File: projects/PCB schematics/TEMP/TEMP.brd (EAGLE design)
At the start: 0 parts

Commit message: POWER - Initial drafts.
Adding in initial place holders for DCDC, 5V, and 12V. Completed most of TEMP.
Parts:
- added IC1, IC10, IC2, IC3, IC4, IC5, IC6, IC7, IC8, IC9: 4051D, 40xx:SO16
- added J1, J2: SAMTEC-TFM-120-02-X-D-LCJ, SAMTEC-TFM-120-02-X-D-LC:SAMTEC-TFM-120-02-X-D-LC
- added R1, R2, R3, R4: (no value), rcl:R0805
- added X2: 5566-4, con-molex:5566-4
- added X3: 5566-2, con-molex:5566-2
- added X4: 5566-10, con-molex:5566-10
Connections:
- new net CS_A: IC1.11, IC10.11, IC2.11, IC3.11, IC4.11, IC5.11, IC6.11, IC7.11, IC8.11, IC9.11, R2.2, X2.1
- new net CS_B: IC1.10, IC10.10, IC2.10, IC3.10, IC4.10, IC5.10, IC6.10, IC7.10, IC8.10, IC9.10, R3.2, X2.2
- new net CS_C: IC1.9, IC10.9, IC2.9, IC3.9, IC4.9, IC5.9, IC6.9, IC7.9, IC8.9, IC9.9, R4.2, X2.3
- new net GND: IC1.8, IC10.8, IC2.8, IC3.8, IC4.8, IC5.8, IC6.8, IC7.8, IC8.8, IC9.8, R1.1, R2.1, R3.1, R4.1, X3.2
- new net INH: IC1.6, IC10.6, IC2.6, IC3.6, IC4.6, IC5.6, IC6.6, IC7.6, IC8.6, IC9.6, R1.2
- new net TEMP1: IC1.13, J1.1
- new net TEMP10: IC2.14, J1.10
- new net TEMP11: IC2.15, J1.11
- new net TEMP12: IC2.12, J1.12
- new net TEMP13: IC2.1, J1.13
- new net TEMP14: IC2.5, J1.14
- new net TEMP15: IC2.2, J1.15
- new net TEMP16: IC2.4, J1.16
- new net TEMP17: IC3.13, J1.17
- new net TEMP18: IC3.14, J1.18
- new net TEMP19: IC3.15, J1.19
- new net TEMP2: IC1.14, J1.2
- new net TEMP20: IC3.12, J1.20
- new net TEMP21: IC3.1, J1.21
- new net TEMP22: IC3.5, J1.22
- new net TEMP23: IC3.2, J1.23
- new net TEMP24: IC3.4, J1.24
- new net TEMP25: IC5.13, J1.25
- new net TEMP26: IC5.14, J1.26
- new net TEMP27: IC5.15, J1.27
- new net TEMP28: IC5.12, J1.28
- new net TEMP29: IC5.1, J1.29
- new net TEMP3: IC1.15, J1.3
- new net TEMP30: IC5.5, J1.30
- new net TEMP31: IC5.2, J1.31
- new net TEMP32: IC5.4, J1.32
- new net TEMP33: IC6.13, J1.33
- new net TEMP34: IC6.14, J1.34
- new net TEMP35: IC6.15, J1.35
- new net TEMP36: IC6.12, J1.36
- new net TEMP37: IC6.1, J1.37
- new net TEMP38: IC6.5, J1.38
- new net TEMP39: IC6.2, J1.39
- new net TEMP4: IC1.12, J1.4
- new net TEMP40: IC6.4, J1.40
- new net TEMP41: IC7.13, J2.1
- new net TEMP42: IC7.14, J2.2
- new net TEMP43: IC7.15, J2.3
- new net TEMP44: IC7.12, J2.4
- new net TEMP45: IC7.1, J2.5
- new net TEMP46: IC7.5, J2.6
- new net TEMP47: IC7.2, J2.7
- new net TEMP48: IC7.4, J2.8
- new net TEMP49: IC4.13, J2.9
- new net TEMP5: IC1.1, J1.5
- new net TEMP50: IC4.14, J2.10
- new net TEMP51: IC4.15, J2.11
- new net TEMP52: IC4.12, J2.12
- new net TEMP53: IC4.1, J2.13
- new net TEMP54: IC4.5, J2.14
- new net TEMP55: IC4.2, J2.15
- new net TEMP56: IC4.4, J2.16
- new net TEMP57: IC9.13, J2.17
- new net TEMP58: IC9.14, J2.18
- new net TEMP59: IC9.15, J2.19
- new net TEMP6: IC1.5, J1.6
- new net TEMP60: IC9.12, J2.20
- new net TEMP61: IC9.1, J2.21
- new net TEMP62: IC9.5, J2.22
- new net TEMP63: IC9.2, J2.23
- new net TEMP64: IC9.4, J2.24
- new net TEMP65: IC8.13, J2.25
- new net TEMP66: IC8.14, J2.26
- new net TEMP67: IC8.15, J2.27
- new net TEMP68: IC8.12, J2.28
- new net TEMP69: IC8.1, J2.29
- new net TEMP7: IC1.2, J1.7
- new net TEMP70: IC8.5, J2.30
- new net TEMP71: IC8.2, J2.31
- new net TEMP72: IC8.4, J2.32
- new net TEMP73: IC10.13, J2.33
- new net TEMP74: IC10.14, J2.34
- new net TEMP75: IC10.15, J2.35
- new net TEMP76: IC10.12, J2.36
- new net TEMP77: IC10.1, J2.37
- new net TEMP78: IC10.5, J2.38
- new net TEMP79: IC10.2, J2.39
- new net TEMP8: IC1.4, J1.8
- new net TEMP80: IC10.4, J2.40
- new net TEMP9: IC2.13, J1.9
- new net TEMP_OUT1: IC1.3, X4.1
- new net TEMP_OUT10: IC10.3, X4.10
- new net TEMP_OUT2: IC2.3, X4.2
- new net TEMP_OUT3: IC3.3, X4.3
- new net TEMP_OUT4: IC5.3, X4.4
- new net TEMP_OUT5: IC6.3, X4.5
- new net TEMP_OUT6: IC7.3, X4.6
- new net TEMP_OUT7: IC4.3, X4.7
- new net TEMP_OUT8: IC9.3, X4.8
- new net TEMP_OUT9: IC8.3, X4.9
- new net VCC: IC1.16, IC10.16, IC2.16, IC3.16, IC4.16, IC5.16, IC6.16, IC7.16, IC8.16, IC9.16, X3.1
- new net VEE: IC1.7, IC10.7, IC2.7, IC3.7, IC4.7, IC5.7, IC6.7, IC7.7, IC8.7, IC9.7
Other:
- board outline added: 78.7 x 64.8 mm

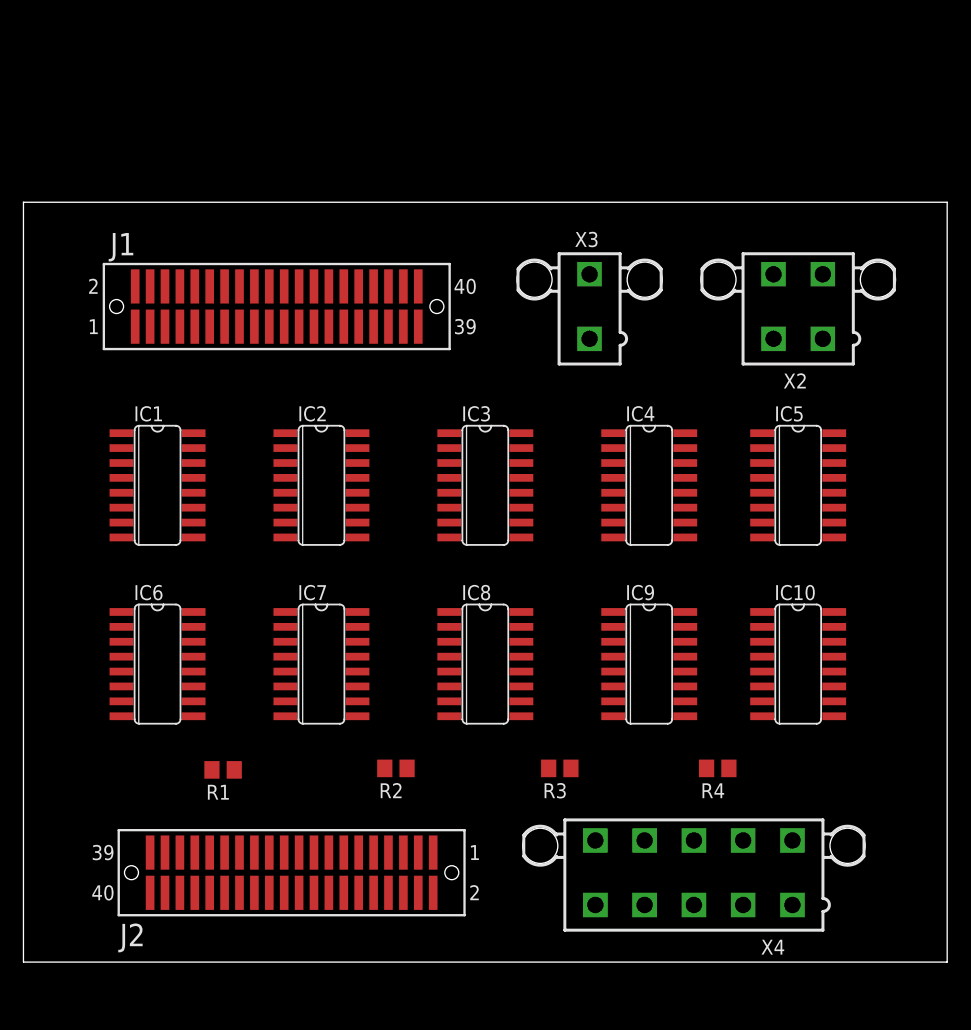
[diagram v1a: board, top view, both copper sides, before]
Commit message: PROJ - Added IMD, OUTPUT.
Additional changes made to INPUT.
OUTPUT board added for ECU/motor controller signal processing.
IMD added for IMD fuse board. Rules may require fusing IMD. Might as well.
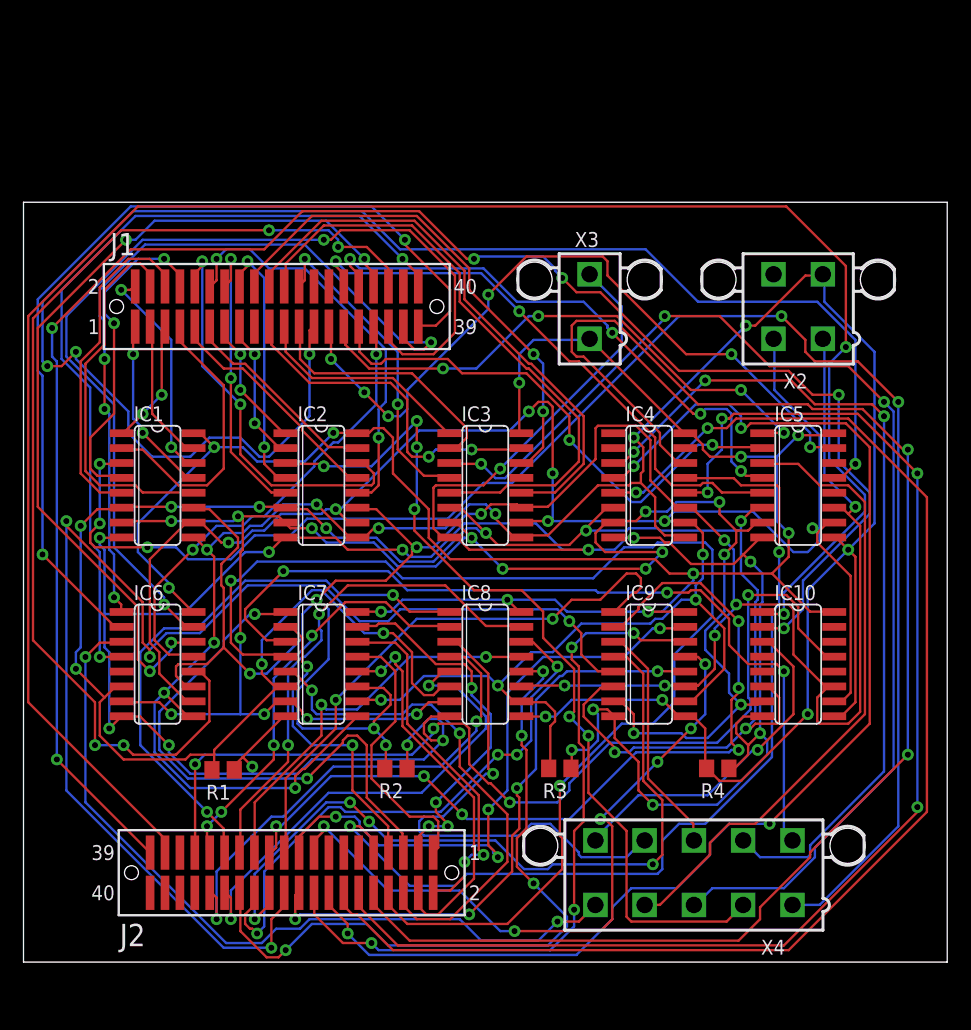
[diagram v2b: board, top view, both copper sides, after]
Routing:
- net GND: track 0.00 -> 240.1 mm, vias 0 -> 16
- net CS_C: track 0.00 -> 215.0 mm, vias 0 -> 13
- net CS_A: track 0.00 -> 205.5 mm, vias 0 -> 12
- net CS_B: track 0.00 -> 199.0 mm, vias 0 -> 11
- net INH: track 0.00 -> 187.8 mm, vias 0 -> 12
- net VCC: track 0.00 -> 171.8 mm, vias 0 -> 11
- net TEMP77: track 0.00 -> 162.7 mm, vias 0 -> 2
- net VEE: track 0.00 -> 158.2 mm, vias 0 -> 17
- net TEMP79: track 0.00 -> 152.1 mm, vias 0 -> 6
- net TEMP_OUT1: track 0.00 -> 138.6 mm, vias 0 -> 5
- net TEMP25: track 0.00 -> 134.1 mm, vias 0 -> 4
- net TEMP50: track 0.00 -> 131.0 mm, vias 0 -> 2
- net TEMP54: track 0.00 -> 116.3 mm, vias 0 -> 2
- net TEMP62: track 0.00 -> 113.0 mm, vias 0 -> 4
- net TEMP52: track 0.00 -> 111.4 mm, vias 0 -> 4
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
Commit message: TEMP - Initial board placement.
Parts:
- removed IC1, IC10, IC2, IC3, IC4, IC5, IC6, IC7, IC8, IC9: 4051D, 40xx:SO16
- removed J2: SAMTEC-TFM-120-02-X-D-LCJ, SAMTEC-TFM-120-02-X-D-LC:SAMTEC-TFM-120-02-X-D-LC
- added MUX1, MUX2, MUX3, MUX4, MUX5: 4051D, 40xx:SO16
- added SH1, SH2, SH3: SHORTT5, shorts:SHORT_TOP-50
- added X1: 5566-4, con-molex:5566-4
- R1, R2, R3, R4: value (none) -> 50k
- X4: value 5566-10 -> 5566-6; device con-molex:5566-10 -> con-molex:5566-6
- moved X3 57.8 mm to (16.5, 7.62), turned to 180 degrees
- moved R4 24.9 mm to (34.3, 15.3)
- moved X2 24.4 mm to (50.8, 36.8), turned to 270 degrees
- moved X4 20.3 mm to (36.8, 7.62), turned to 180 degrees
- moved R1 20.0 mm to (34.2, 26.6)
- moved J1 12.7 mm to (31.8, 48.3)
- moved R3 11.7 mm to (34.3, 19.1)
- moved R2 6.84 mm to (34.3, 22.9)
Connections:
- removed net CS_A: IC1.11, IC10.11, IC2.11, IC3.11, IC4.11, IC5.11, IC6.11, IC7.11, IC8.11, IC9.11, R2.2, X2.1
- removed net CS_B: IC1.10, IC10.10, IC2.10, IC3.10, IC4.10, IC5.10, IC6.10, IC7.10, IC8.10, IC9.10, R3.2, X2.2
- removed net CS_C: IC1.9, IC10.9, IC2.9, IC3.9, IC4.9, IC5.9, IC6.9, IC7.9, IC8.9, IC9.9, R4.2, X2.3
- removed net TEMP41: IC7.13, J2.1
- removed net TEMP42: IC7.14, J2.2
- removed net TEMP43: IC7.15, J2.3
- removed net TEMP44: IC7.12, J2.4
- removed net TEMP45: IC7.1, J2.5
- removed net TEMP46: IC7.5, J2.6
- removed net TEMP47: IC7.2, J2.7
- removed net TEMP48: IC7.4, J2.8
- removed net TEMP49: IC4.13, J2.9
- removed net TEMP50: IC4.14, J2.10
- removed net TEMP51: IC4.15, J2.11
- removed net TEMP52: IC4.12, J2.12
- removed net TEMP53: IC4.1, J2.13
- removed net TEMP54: IC4.5, J2.14
- removed net TEMP55: IC4.2, J2.15
- removed net TEMP56: IC4.4, J2.16
- removed net TEMP57: IC9.13, J2.17
- removed net TEMP58: IC9.14, J2.18
- removed net TEMP59: IC9.15, J2.19
- removed net TEMP60: IC9.12, J2.20
- removed net TEMP61: IC9.1, J2.21
- removed net TEMP62: IC9.5, J2.22
- removed net TEMP63: IC9.2, J2.23
- removed net TEMP64: IC9.4, J2.24
- removed net TEMP65: IC8.13, J2.25
- removed net TEMP66: IC8.14, J2.26
- removed net TEMP67: IC8.15, J2.27
- removed net TEMP68: IC8.12, J2.28
- removed net TEMP69: IC8.1, J2.29
- removed net TEMP70: IC8.5, J2.30
- removed net TEMP71: IC8.2, J2.31
- removed net TEMP72: IC8.4, J2.32
- removed net TEMP73: IC10.13, J2.33
- removed net TEMP74: IC10.14, J2.34
- removed net TEMP75: IC10.15, J2.35
- removed net TEMP76: IC10.12, J2.36
- removed net TEMP77: IC10.1, J2.37
- removed net TEMP78: IC10.5, J2.38
- removed net TEMP79: IC10.2, J2.39
- removed net TEMP80: IC10.4, J2.40
- removed net TEMP_OUT10: IC10.3, X4.10
- removed net TEMP_OUT6: IC7.3, X4.6
- removed net TEMP_OUT7: IC4.3, X4.7
- removed net TEMP_OUT8: IC9.3, X4.8
- removed net TEMP_OUT9: IC8.3, X4.9
- removed net VEE: IC1.7, IC10.7, IC2.7, IC3.7, IC4.7, IC5.7, IC6.7, IC7.7, IC8.7, IC9.7
- new net CS_A_IN: MUX1.11, MUX2.11, MUX3.11, MUX4.11, MUX5.11, R2.2, SH1.1, X2.1
- new net CS_A_OUT: SH1.2, X1.1
- new net CS_B_IN: MUX1.10, MUX2.10, MUX3.10, MUX4.10, MUX5.10, R3.2, SH2.1, X2.2
- new net CS_B_OUT: SH2.2, X1.2
- new net CS_C_IN: MUX1.9, MUX2.9, MUX3.9, MUX4.9, MUX5.9, R4.2, SH3.1, X2.3
- new net CS_C_OUT: SH3.2, X1.3
- net GND: now also MUX1.7, MUX1.8, MUX2.7, MUX2.8, MUX3.7, MUX3.8, MUX4.7, MUX4.8, MUX5.7, MUX5.8; no longer IC1.8, IC10.8, IC2.8, IC3.8, IC4.8, IC5.8, IC6.8, IC7.8, IC8.8, IC9.8
- net INH: now also MUX1.6, MUX2.6, MUX3.6, MUX4.6, MUX5.6; no longer IC1.6, IC10.6, IC2.6, IC3.6, IC4.6, IC5.6, IC6.6, IC7.6, IC8.6, IC9.6
- net TEMP1: now also MUX1.13; no longer IC1.13
- net TEMP10: now also MUX2.14; no longer IC2.14
- net TEMP11: now also MUX2.15; no longer IC2.15
- net TEMP12: now also MUX2.12; no longer IC2.12
- net TEMP13: now also MUX2.1; no longer IC2.1
- net TEMP14: now also MUX2.5; no longer IC2.5
- net TEMP15: now also MUX2.2; no longer IC2.2
- net TEMP16: now also MUX2.4; no longer IC2.4
- net TEMP17: now also MUX3.13; no longer IC3.13
- net TEMP18: now also MUX3.14; no longer IC3.14
- net TEMP19: now also MUX3.15; no longer IC3.15
- net TEMP2: now also MUX1.14; no longer IC1.14
- net TEMP20: now also MUX3.12; no longer IC3.12
- net TEMP21: now also MUX3.1; no longer IC3.1
- net TEMP22: now also MUX3.5; no longer IC3.5
- net TEMP23: now also MUX3.2; no longer IC3.2
- net TEMP24: now also MUX3.4; no longer IC3.4
- net TEMP25: now also MUX4.13; no longer IC5.13
- net TEMP26: now also MUX4.14; no longer IC5.14
- net TEMP27: now also MUX4.15; no longer IC5.15
- net TEMP28: now also MUX4.12; no longer IC5.12
- net TEMP29: now also MUX4.1; no longer IC5.1
- net TEMP3: now also MUX1.15; no longer IC1.15
- net TEMP30: now also MUX4.5; no longer IC5.5
- net TEMP31: now also MUX4.2; no longer IC5.2
- net TEMP32: now also MUX4.4; no longer IC5.4
- net TEMP33: now also MUX5.13; no longer IC6.13
- net TEMP34: now also MUX5.14; no longer IC6.14
- net TEMP35: now also MUX5.15; no longer IC6.15
- net TEMP36: now also MUX5.12; no longer IC6.12
- net TEMP37: now also MUX5.1; no longer IC6.1
- net TEMP38: now also MUX5.5; no longer IC6.5
- net TEMP39: now also MUX5.2; no longer IC6.2
- net TEMP4: now also MUX1.12; no longer IC1.12
- net TEMP40: now also MUX5.4; no longer IC6.4
- net TEMP5: now also MUX1.1; no longer IC1.1
- net TEMP6: now also MUX1.5; no longer IC1.5
- net TEMP7: now also MUX1.2; no longer IC1.2
- net TEMP8: now also MUX1.4; no longer IC1.4
- net TEMP9: now also MUX2.13; no longer IC2.13
- net TEMP_OUT1: now also MUX1.3; no longer IC1.3
- net TEMP_OUT2: now also MUX2.3; no longer IC2.3
- net TEMP_OUT3: now also MUX3.3; no longer IC3.3
- net TEMP_OUT4: now also MUX4.3; no longer IC5.3
- net TEMP_OUT5: now also MUX5.3; no longer IC6.3
- net VCC: now also MUX1.16, MUX2.16, MUX3.16, MUX4.16, MUX5.16; no longer IC1.16, IC10.16, IC2.16, IC3.16, IC4.16, IC5.16, IC6.16, IC7.16, IC8.16, IC9.16
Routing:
- net GND: track 240.1 -> 6.35 mm, vias 16 -> 0
- net CS_C: track 215.0 -> 0.00 mm, vias 13 -> 0
- net CS_A: track 205.5 -> 0.00 mm, vias 12 -> 0
- net CS_B: track 199.0 -> 0.00 mm, vias 11 -> 0
- net TEMP77: track 162.7 -> 0.00 mm, vias 2 -> 0
- net VEE: track 158.2 -> 0.00 mm, vias 17 -> 0
- net TEMP79: track 152.1 -> 0.00 mm, vias 6 -> 0
- net TEMP25: track 134.1 -> 0.00 mm, vias 4 -> 0
- net TEMP50: track 131.0 -> 0.00 mm, vias 2 -> 0
- net INH: track 187.8 -> 67.2 mm, vias 12 -> 0
- net TEMP54: track 116.3 -> 0.00 mm, vias 2 -> 0
- net TEMP62: track 113.0 -> 0.00 mm, vias 4 -> 0
- net TEMP52: track 111.4 -> 0.00 mm, vias 4 -> 0
- net TEMP56: track 109.3 -> 0.00 mm, vias 4 -> 0
- net TEMP48: track 107.0 -> 0.00 mm, vias 2 -> 0
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- added copper zone on layer 1, net GND
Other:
- board size 78.7 x 64.8 mm -> 58.4 x 54.6 mm
